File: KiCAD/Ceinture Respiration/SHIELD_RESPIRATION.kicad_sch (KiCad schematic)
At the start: 9 parts, among them J1 DIN-8, J2 DIN-8

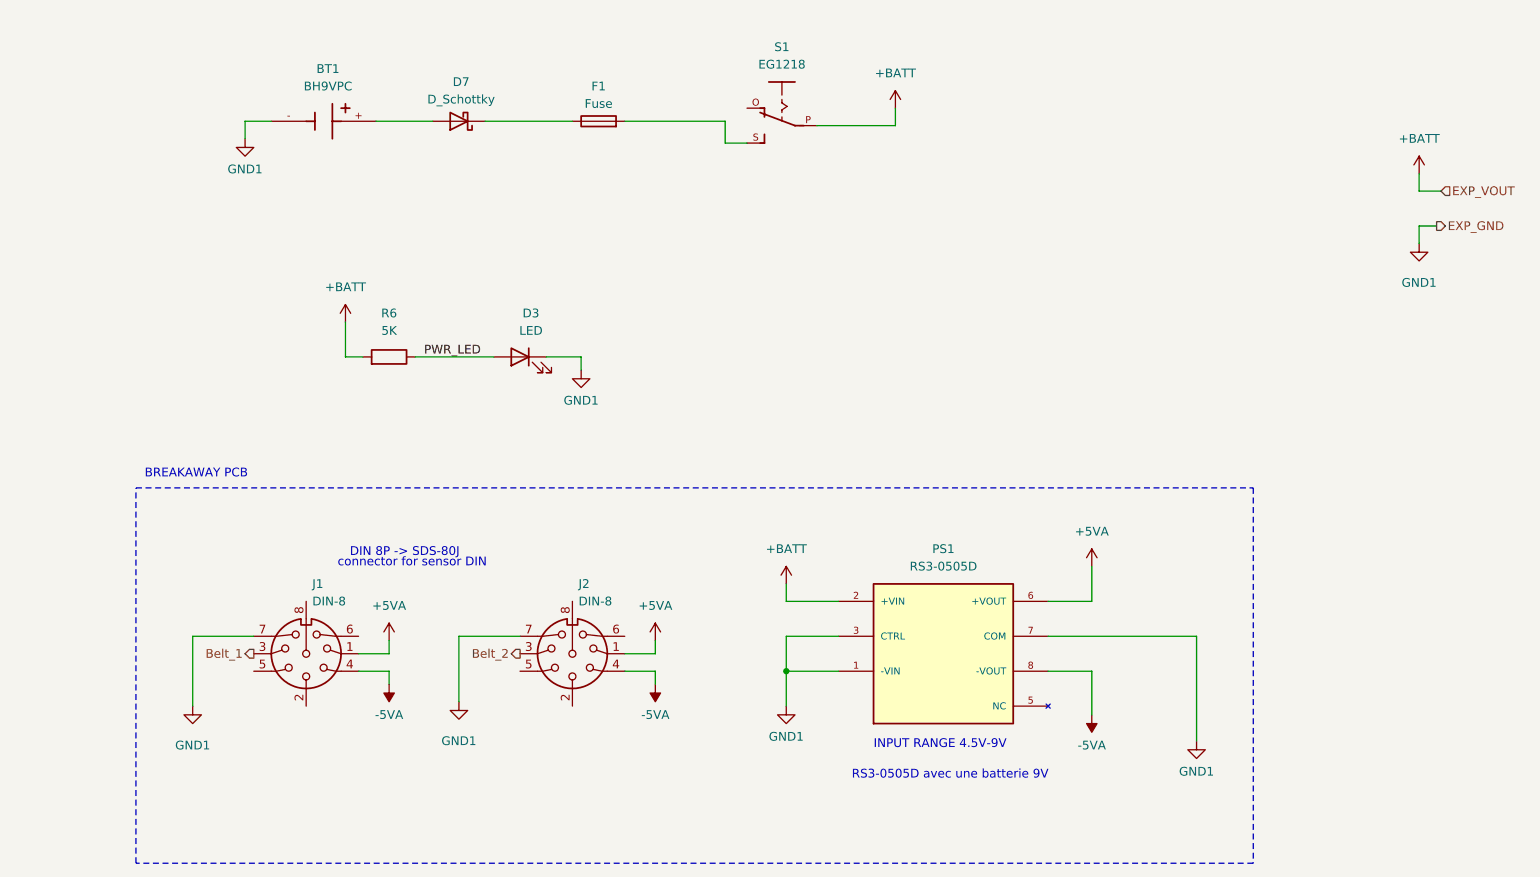
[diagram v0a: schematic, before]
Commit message: Schematique 99%, PCB 50%
schématique complété, nettoyé et layout complété, reste routage
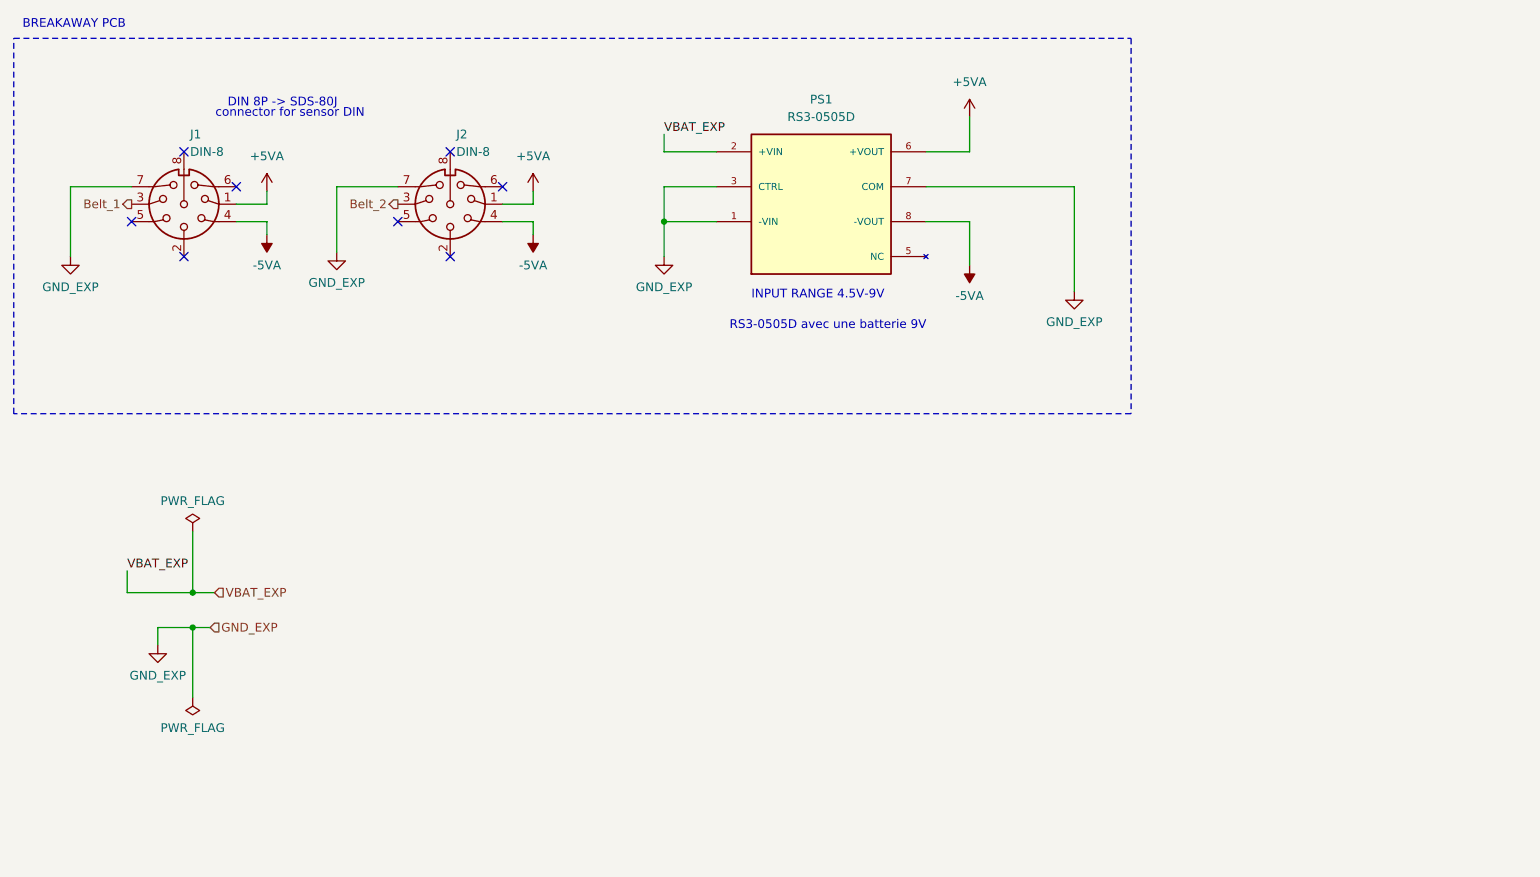
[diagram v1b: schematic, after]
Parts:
- removed BT1: BH9VPC, CentureResp:BAT_BH9VPC, symbol CeintureRespAT:BH9VPC
- removed D3: LED, LED_THT:LED_D3.0mm, symbol Device:LED
- removed D7: D_Schottky, Diode_SMD:D_SOD-123, symbol Device:D_Schottky
- removed F1: Fuse, symbol Device:Fuse
- removed R6: 5K, Resistor_SMD:R_0603_1608Metric, symbol Device:R
- removed S1: EG1218, CentureResp:EG1218, symbol CeintureRespAT:EG1218
- J1, J2: Digikey (none) -> CP-2380-ND
- PS1: Digikey (none) -> 945-1318-ND
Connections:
- net +BATT renamed VBAT_EXP
- net GND1 renamed GND_EXP
- no-connect marks 0 -> 8
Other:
- company: (none) -> IngRéadapt UL
- moved on the sheet: J1, J2, PS1
